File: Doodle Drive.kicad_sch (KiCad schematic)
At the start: 37 parts, among them J1 USB_B, J2 PINHD_1x4_Male, J3 Screw_Terminal_01x02, J6 PINHD_1x2_Male, SW1 Push_Button, SW2 Push_Button, SW3 Push_Button, U1 STM32F411RETx, U6 AP7343-33W5-7, U7 CP2102-GMR, Y1 32.768KHz ±20ppm 12.5pF, Y2 25MHZ 12PF

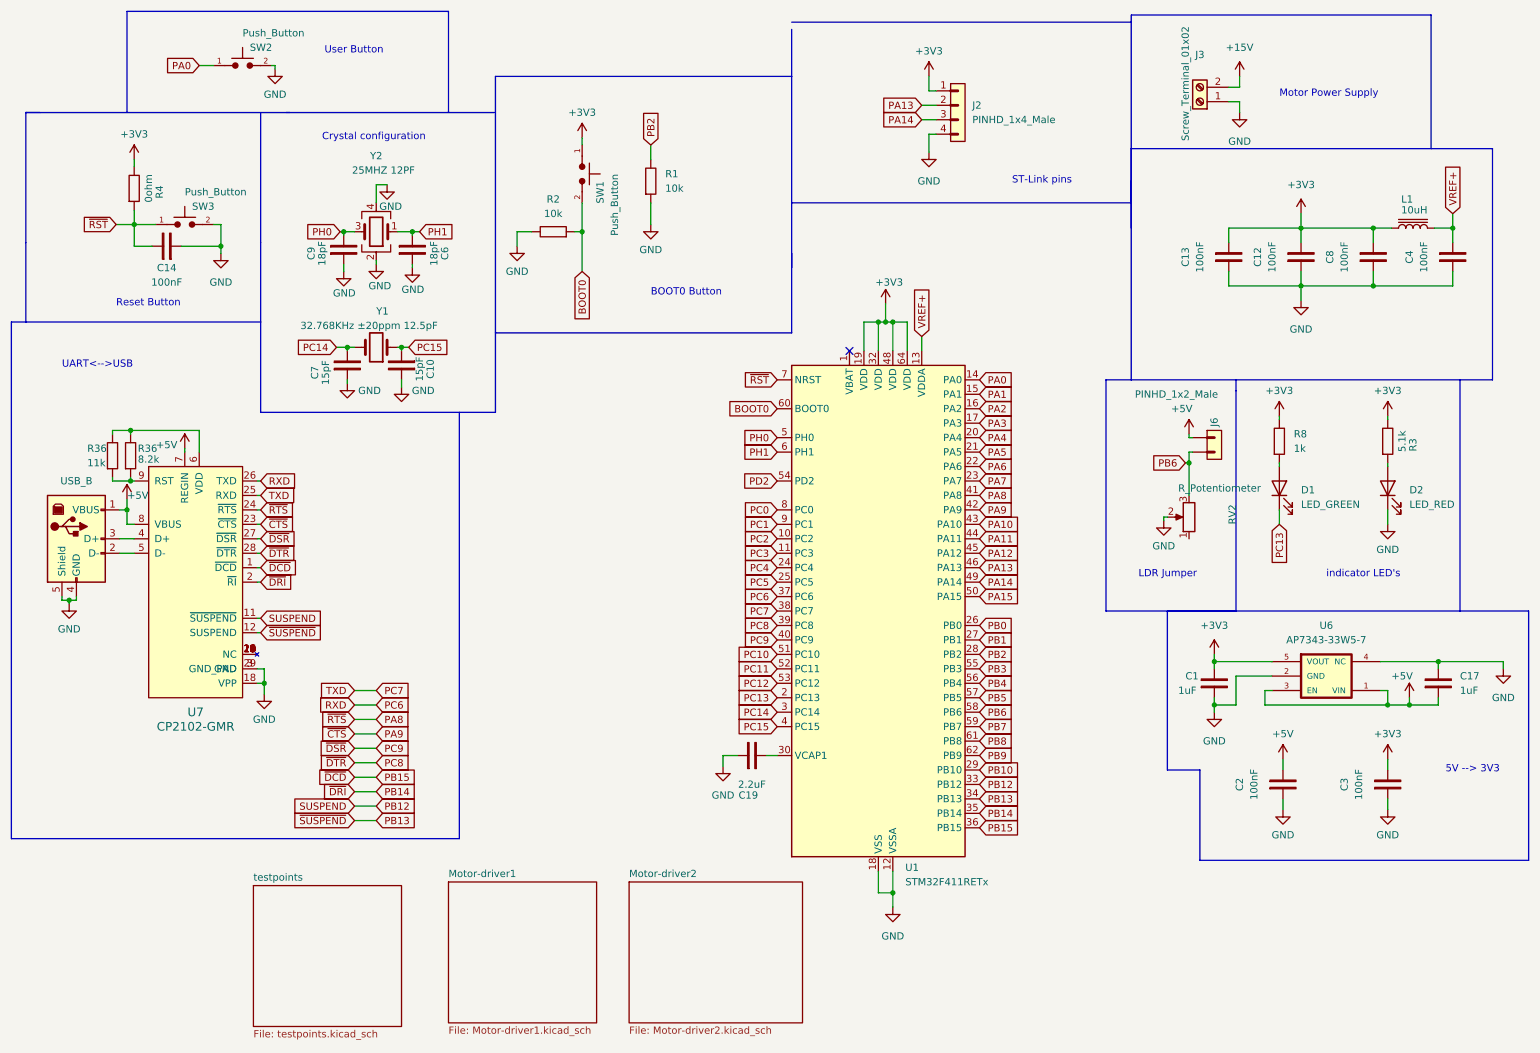
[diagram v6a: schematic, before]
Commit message: placed jlcpcb basic buttons and rerouted unchristliche wires
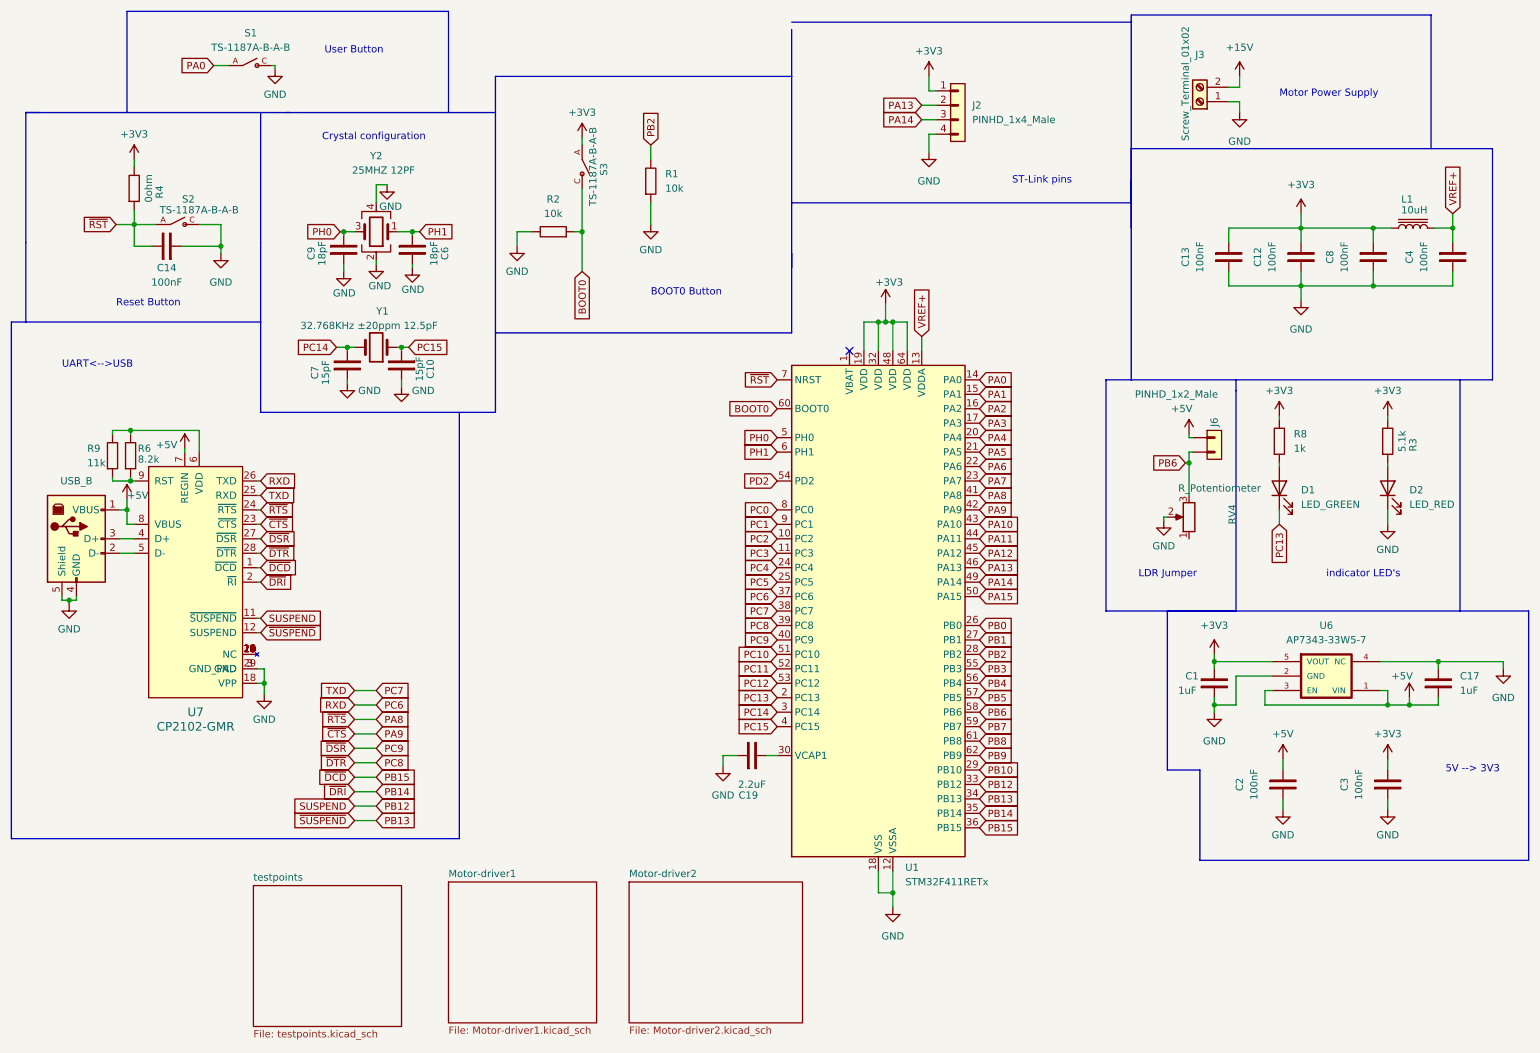
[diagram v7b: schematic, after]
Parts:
- removed SW1, SW2, SW3: Push_Button, Button_Switch_SMD:SW_SPST_B3U-1000P, symbol PCM_SL_Devices:Push_Button
- added S1, S2, S3: TS-1187A-B-A-B, TS-1187A-B-A-B:SW_TS-1187A-B-A-B, symbol TS-1187A-B-A-B:TS-1187A-B-A-B
- renumbered R36 to R6, R36 to R9, RV2 to RV4
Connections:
- net +3V3: now also S3.A
- net BOOT0: now also S3.C
- net GND: now also S1.C, S2.C
- net PA0: now also S1.A
- net ~{RST}: now also S2.A

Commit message: moved every third party content to lib, added 3d models and also just finished rerouting EVERYTHING. also added pcb addon for st-link so i dont accidentally verole anymore
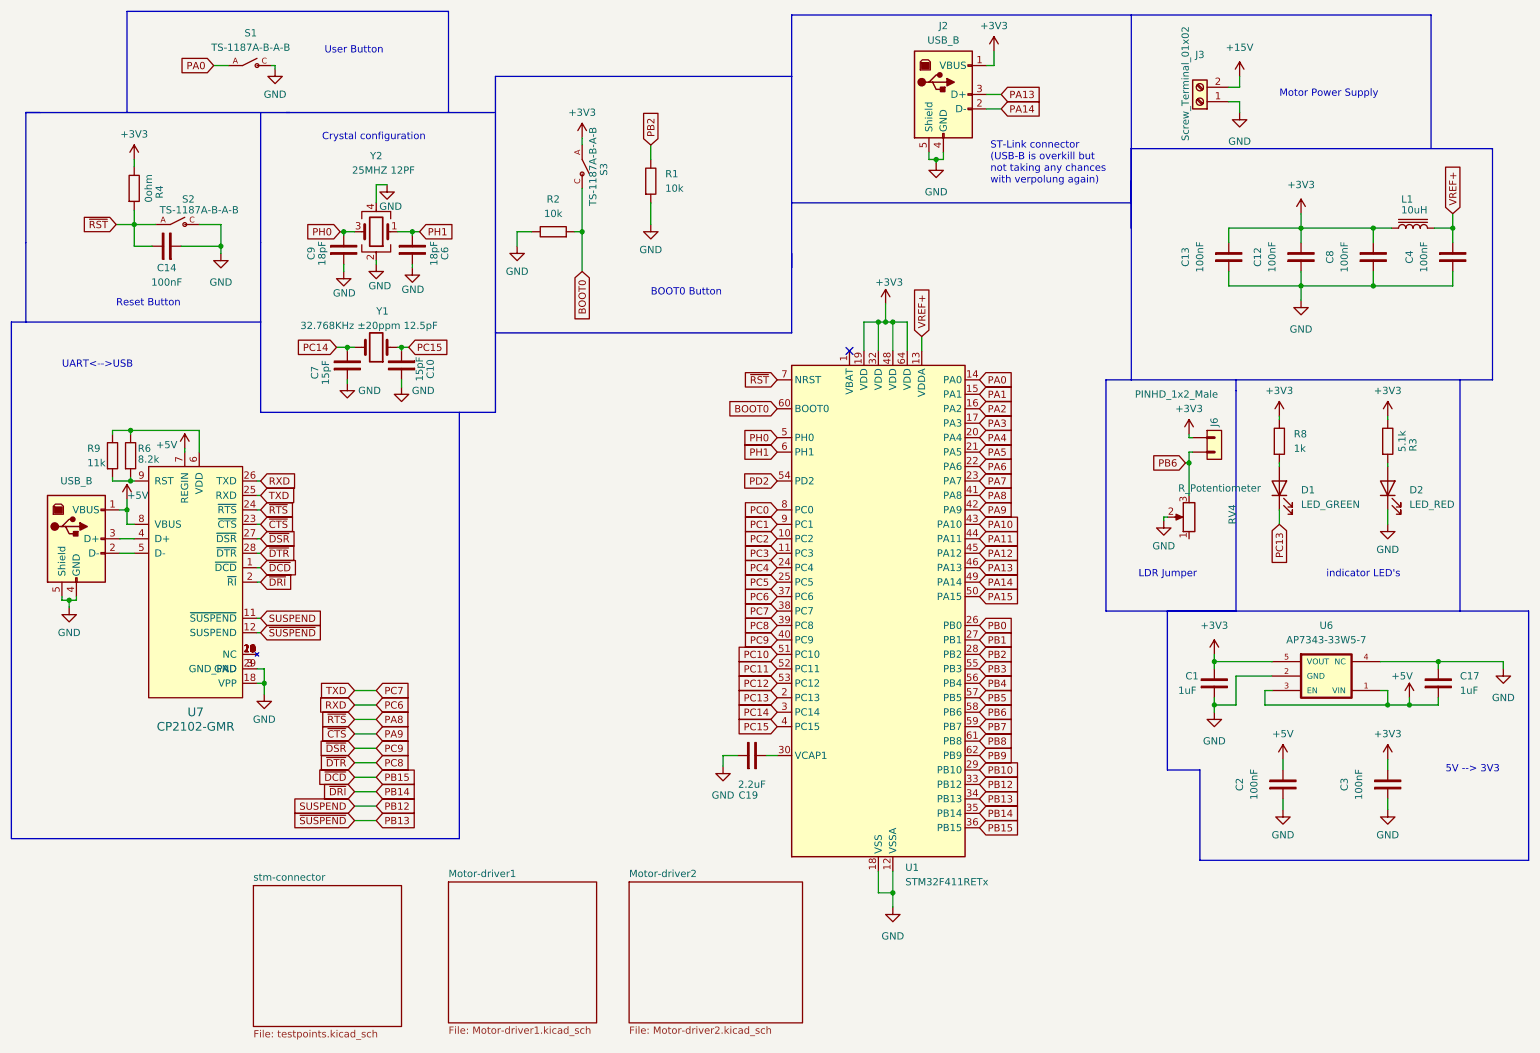
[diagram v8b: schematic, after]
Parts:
- removed J2: PINHD_1x4_Male, Connector_PinHeader_2.54mm:PinHeader_1x04_P2.54mm_Vertical, symbol PCM_SL_Pin_Headers:PINHD_1x4_Male
- added J2: USB_B, Connector_USB:USB_B_Lumberg_2411_02_Horizontal, symbol Connector:USB_B
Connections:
- net +3V3: now also J6.1, J2.1 (VBUS)
- net +5V: no longer J6.1
- net GND: now also J2.4 (GND), J2.5 (Shield)
- net PA13: now also J2.3 (D+)
- net PA14: now also J2.2 (D-)
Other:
- sheet testpoints renamed stm-connector
- note added: "ST-Link connector (USB-B is overkill but not taking any chances with verpolung again)"
- note removed: "ST-Link pins"
